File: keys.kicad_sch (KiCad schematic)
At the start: 13 parts, among them SW1 Esc, SW10 F9, SW11 F10, SW12 F11, SW13 F12, SW2 F1, SW3 F2, SW4 F3, SW5 F4, SW6 F5, SW7 F6, SW8 F7, SW9 F8

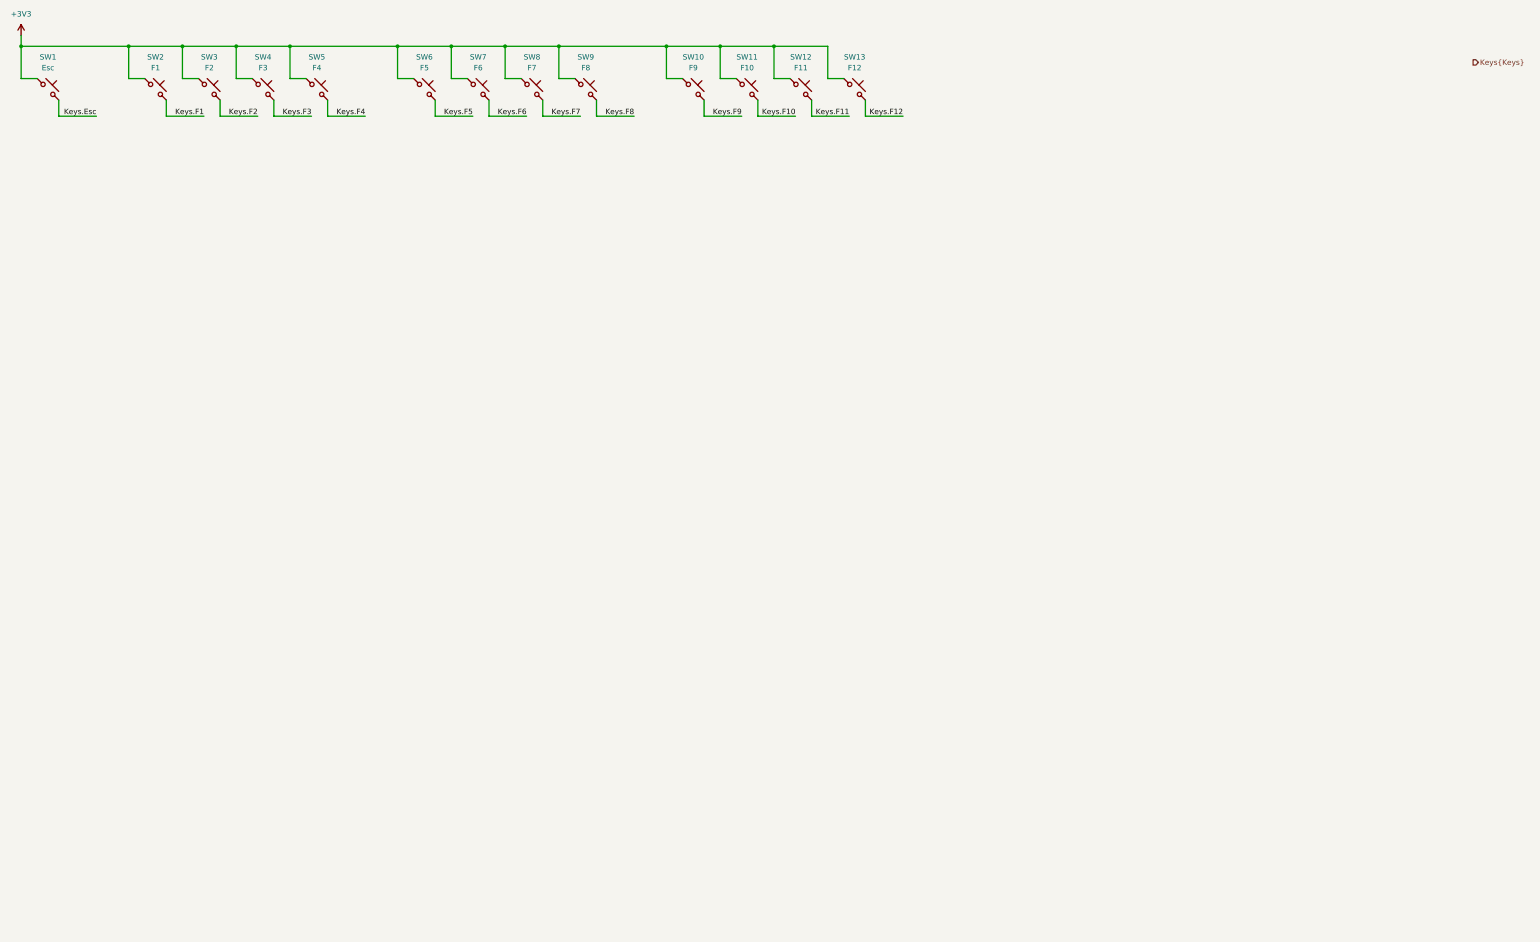
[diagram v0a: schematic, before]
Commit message: Add all keys
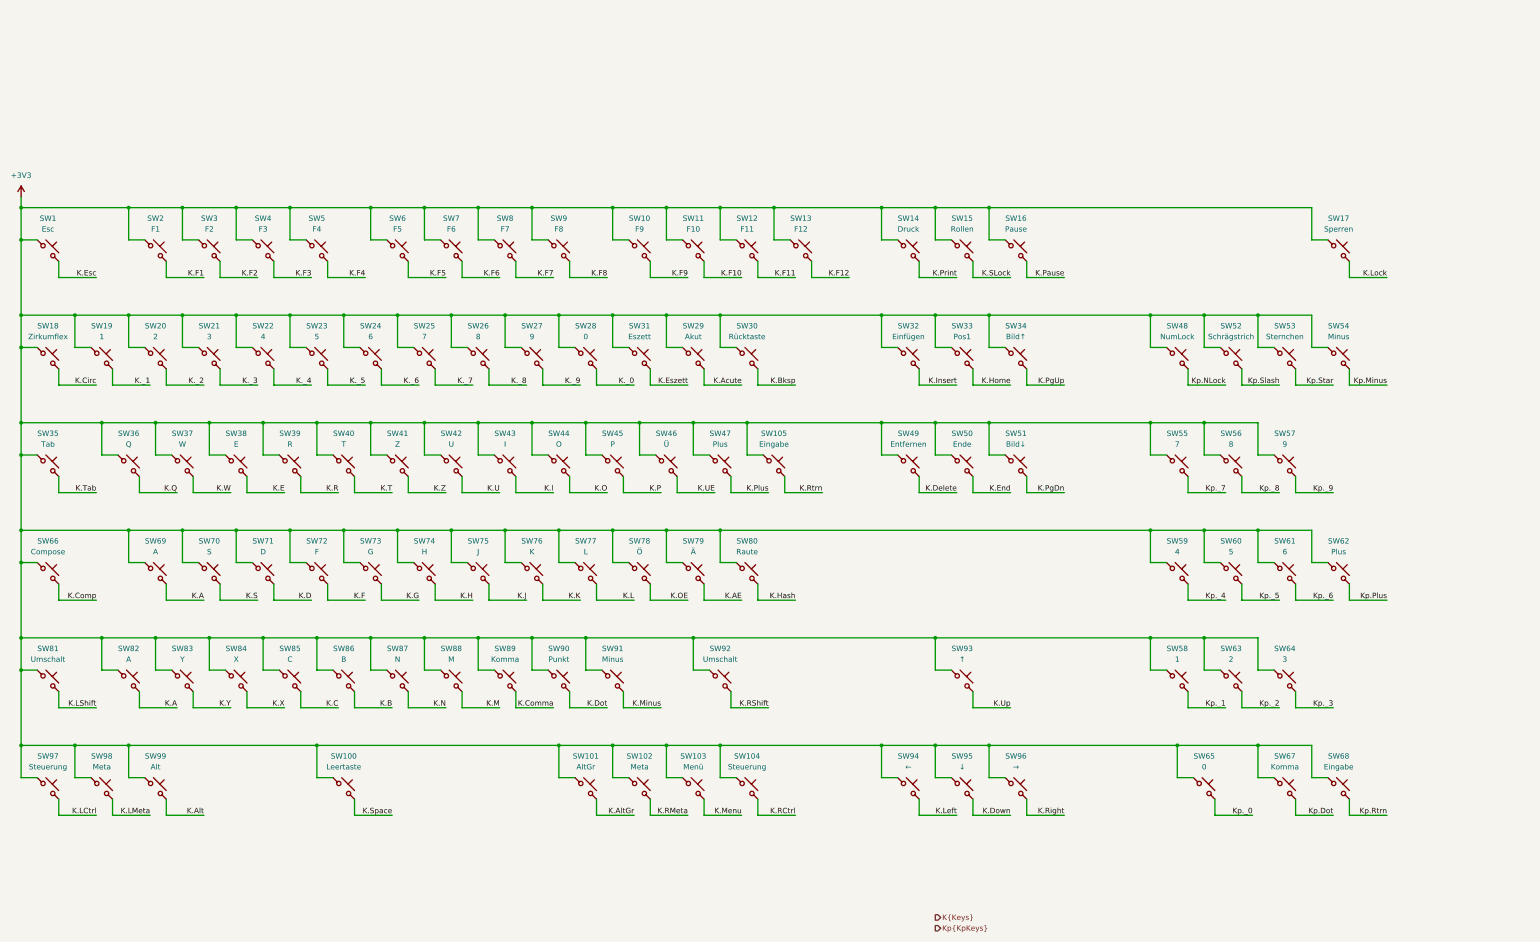
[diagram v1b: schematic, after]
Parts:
- added SW100: Leertaste, Button_Switch_Keyboard:SW_Cherry_MX_6.25u_PCB, symbol Switch:SW_Push_45deg
- added SW101: AltGr, Button_Switch_Keyboard:SW_Cherry_MX_1.25u_PCB, symbol Switch:SW_Push_45deg
- added SW102, SW98: Meta, Button_Switch_Keyboard:SW_Cherry_MX_1.25u_PCB, symbol Switch:SW_Push_45deg
- added SW103: Menü, Button_Switch_Keyboard:SW_Cherry_MX_1.25u_PCB, symbol Switch:SW_Push_45deg
- added SW104, SW97: Steuerung, Button_Switch_Keyboard:SW_Cherry_MX_1.25u_PCB, symbol Switch:SW_Push_45deg
- added SW105: Eingabe, Button_Switch_Keyboard:SW_Cherry_MX_ISOEnter_PCB, symbol Switch:SW_Push_45deg
- added SW14: Druck, Button_Switch_Keyboard:SW_Cherry_MX_1.00u_PCB, symbol Switch:SW_Push_45deg
- added SW15: Rollen, Button_Switch_Keyboard:SW_Cherry_MX_1.00u_PCB, symbol Switch:SW_Push_45deg
- added SW16: Pause, Button_Switch_Keyboard:SW_Cherry_MX_1.00u_PCB, symbol Switch:SW_Push_45deg
- added SW17: Sperren, Button_Switch_Keyboard:SW_Cherry_MX_1.00u_PCB, symbol Switch:SW_Push_45deg
- added SW18: Zirkumflex, Button_Switch_Keyboard:SW_Cherry_MX_1.00u_PCB, symbol Switch:SW_Push_45deg
- added SW19, SW58: 1, Button_Switch_Keyboard:SW_Cherry_MX_1.00u_PCB, symbol Switch:SW_Push_45deg
- added SW20, SW63: 2, Button_Switch_Keyboard:SW_Cherry_MX_1.00u_PCB, symbol Switch:SW_Push_45deg
- added SW21, SW64: 3, Button_Switch_Keyboard:SW_Cherry_MX_1.00u_PCB, symbol Switch:SW_Push_45deg
- added SW22, SW59: 4, Button_Switch_Keyboard:SW_Cherry_MX_1.00u_PCB, symbol Switch:SW_Push_45deg
- added SW23, SW60: 5, Button_Switch_Keyboard:SW_Cherry_MX_1.00u_PCB, symbol Switch:SW_Push_45deg
- added SW24, SW61: 6, Button_Switch_Keyboard:SW_Cherry_MX_1.00u_PCB, symbol Switch:SW_Push_45deg
- added SW25, SW55: 7, Button_Switch_Keyboard:SW_Cherry_MX_1.00u_PCB, symbol Switch:SW_Push_45deg
- added SW26, SW56: 8, Button_Switch_Keyboard:SW_Cherry_MX_1.00u_PCB, symbol Switch:SW_Push_45deg
- added SW27, SW57: 9, Button_Switch_Keyboard:SW_Cherry_MX_1.00u_PCB, symbol Switch:SW_Push_45deg
- added SW28: 0, Button_Switch_Keyboard:SW_Cherry_MX_1.00u_PCB, symbol Switch:SW_Push_45deg
- added SW29: Akut, Button_Switch_Keyboard:SW_Cherry_MX_1.00u_PCB, symbol Switch:SW_Push_45deg
- added SW30: Rücktaste, Button_Switch_Keyboard:SW_Cherry_MX_2.00u_PCB, symbol Switch:SW_Push_45deg
- added SW31: Eszett, Button_Switch_Keyboard:SW_Cherry_MX_1.00u_PCB, symbol Switch:SW_Push_45deg
- added SW32: Einfügen, Button_Switch_Keyboard:SW_Cherry_MX_1.00u_PCB, symbol Switch:SW_Push_45deg
- added SW33: Pos1, Button_Switch_Keyboard:SW_Cherry_MX_1.00u_PCB, symbol Switch:SW_Push_45deg
- added SW34: Bild↑, Button_Switch_Keyboard:SW_Cherry_MX_1.00u_PCB, symbol Switch:SW_Push_45deg
- added SW35: Tab, Button_Switch_Keyboard:SW_Cherry_MX_1.50u_PCB, symbol Switch:SW_Push_45deg
- added SW36: Q, Button_Switch_Keyboard:SW_Cherry_MX_1.00u_PCB, symbol Switch:SW_Push_45deg
- added SW37: W, Button_Switch_Keyboard:SW_Cherry_MX_1.00u_PCB, symbol Switch:SW_Push_45deg
- added SW38: E, Button_Switch_Keyboard:SW_Cherry_MX_1.00u_PCB, symbol Switch:SW_Push_45deg
- added SW39: R, Button_Switch_Keyboard:SW_Cherry_MX_1.00u_PCB, symbol Switch:SW_Push_45deg
- added SW40: T, Button_Switch_Keyboard:SW_Cherry_MX_1.00u_PCB, symbol Switch:SW_Push_45deg
- added SW41: Z, Button_Switch_Keyboard:SW_Cherry_MX_1.00u_PCB, symbol Switch:SW_Push_45deg
- added SW42: U, Button_Switch_Keyboard:SW_Cherry_MX_1.00u_PCB, symbol Switch:SW_Push_45deg
- added SW43: I, Button_Switch_Keyboard:SW_Cherry_MX_1.00u_PCB, symbol Switch:SW_Push_45deg
- added SW44: O, Button_Switch_Keyboard:SW_Cherry_MX_1.00u_PCB, symbol Switch:SW_Push_45deg
- added SW45: P, Button_Switch_Keyboard:SW_Cherry_MX_1.00u_PCB, symbol Switch:SW_Push_45deg
- added SW46: Ü, Button_Switch_Keyboard:SW_Cherry_MX_1.00u_PCB, symbol Switch:SW_Push_45deg
- added SW47: Plus, Button_Switch_Keyboard:SW_Cherry_MX_1.00u_PCB, symbol Switch:SW_Push_45deg
- added SW48: NumLock, Button_Switch_Keyboard:SW_Cherry_MX_1.00u_PCB, symbol Switch:SW_Push_45deg
- added SW49: Entfernen, Button_Switch_Keyboard:SW_Cherry_MX_1.00u_PCB, symbol Switch:SW_Push_45deg
- added SW50: Ende, Button_Switch_Keyboard:SW_Cherry_MX_1.00u_PCB, symbol Switch:SW_Push_45deg
- added SW51: Bild↓, Button_Switch_Keyboard:SW_Cherry_MX_1.00u_PCB, symbol Switch:SW_Push_45deg
- added SW52: Schrägstrich, Button_Switch_Keyboard:SW_Cherry_MX_1.00u_PCB, symbol Switch:SW_Push_45deg
- added SW53: Sternchen, Button_Switch_Keyboard:SW_Cherry_MX_1.00u_PCB, symbol Switch:SW_Push_45deg
- added SW54, SW91: Minus, Button_Switch_Keyboard:SW_Cherry_MX_1.00u_PCB, symbol Switch:SW_Push_45deg
- added SW62: Plus, Button_Switch_Keyboard:SW_Cherry_MX_2.00u_Vertical_PCB, symbol Switch:SW_Push_45deg
- added SW65: 0, Button_Switch_Keyboard:SW_Cherry_MX_2.00u_PCB, symbol Switch:SW_Push_45deg
- added SW66: Compose, Button_Switch_Keyboard:SW_Cherry_MX_1.75u_PCB, symbol Switch:SW_Push_45deg
- added SW67, SW89: Komma, Button_Switch_Keyboard:SW_Cherry_MX_1.00u_PCB, symbol Switch:SW_Push_45deg
- added SW68: Eingabe, Button_Switch_Keyboard:SW_Cherry_MX_2.00u_Vertical_PCB, symbol Switch:SW_Push_45deg
- added SW69, SW82: A, Button_Switch_Keyboard:SW_Cherry_MX_1.00u_PCB, symbol Switch:SW_Push_45deg
- added SW70: S, Button_Switch_Keyboard:SW_Cherry_MX_1.00u_PCB, symbol Switch:SW_Push_45deg
- added SW71: D, Button_Switch_Keyboard:SW_Cherry_MX_1.00u_PCB, symbol Switch:SW_Push_45deg
- added SW72: F, Button_Switch_Keyboard:SW_Cherry_MX_1.00u_PCB, symbol Switch:SW_Push_45deg
- added SW73: G, Button_Switch_Keyboard:SW_Cherry_MX_1.00u_PCB, symbol Switch:SW_Push_45deg
- added SW74: H, Button_Switch_Keyboard:SW_Cherry_MX_1.00u_PCB, symbol Switch:SW_Push_45deg
- added SW75: J, Button_Switch_Keyboard:SW_Cherry_MX_1.00u_PCB, symbol Switch:SW_Push_45deg
- added SW76: K, Button_Switch_Keyboard:SW_Cherry_MX_1.00u_PCB, symbol Switch:SW_Push_45deg
- added SW77: L, Button_Switch_Keyboard:SW_Cherry_MX_1.00u_PCB, symbol Switch:SW_Push_45deg
- added SW78: Ö, Button_Switch_Keyboard:SW_Cherry_MX_1.00u_PCB, symbol Switch:SW_Push_45deg
- added SW79: Ä, Button_Switch_Keyboard:SW_Cherry_MX_1.00u_PCB, symbol Switch:SW_Push_45deg
- added SW80: Raute, Button_Switch_Keyboard:SW_Cherry_MX_1.00u_PCB, symbol Switch:SW_Push_45deg
- added SW81: Umschalt, Button_Switch_Keyboard:SW_Cherry_MX_1.25u_PCB, symbol Switch:SW_Push_45deg
- added SW83: Y, Button_Switch_Keyboard:SW_Cherry_MX_1.00u_PCB, symbol Switch:SW_Push_45deg
- added SW84: X, Button_Switch_Keyboard:SW_Cherry_MX_1.00u_PCB, symbol Switch:SW_Push_45deg
- added SW85: C, Button_Switch_Keyboard:SW_Cherry_MX_1.00u_PCB, symbol Switch:SW_Push_45deg
- added SW86: B, Button_Switch_Keyboard:SW_Cherry_MX_1.00u_PCB, symbol Switch:SW_Push_45deg
- added SW87: N, Button_Switch_Keyboard:SW_Cherry_MX_1.00u_PCB, symbol Switch:SW_Push_45deg
- added SW88: M, Button_Switch_Keyboard:SW_Cherry_MX_1.00u_PCB, symbol Switch:SW_Push_45deg
- added SW90: Punkt, Button_Switch_Keyboard:SW_Cherry_MX_1.00u_PCB, symbol Switch:SW_Push_45deg
- added SW92: Umschalt, Button_Switch_Keyboard:SW_Cherry_MX_2.75u_PCB, symbol Switch:SW_Push_45deg
- added SW93: ↑, Button_Switch_Keyboard:SW_Cherry_MX_1.00u_PCB, symbol Switch:SW_Push_45deg
- added SW94: ←, Button_Switch_Keyboard:SW_Cherry_MX_1.00u_PCB, symbol Switch:SW_Push_45deg
- added SW95: ↓, Button_Switch_Keyboard:SW_Cherry_MX_1.00u_PCB, symbol Switch:SW_Push_45deg
- added SW96: →, Button_Switch_Keyboard:SW_Cherry_MX_1.00u_PCB, symbol Switch:SW_Push_45deg
- added SW99: Alt, Button_Switch_Keyboard:SW_Cherry_MX_1.25u_PCB, symbol Switch:SW_Push_45deg
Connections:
- net +3V3: now also SW100.1, SW101.1, SW102.1, SW103.1, SW104.1, SW105.1, SW14.1, SW15.1, SW16.1, SW17.1, SW18.1, SW19.1, SW20.1, SW21.1, SW22.1, SW23.1, SW24.1, SW25.1, SW26.1, SW27.1, SW28.1, SW29.1, SW30.1, SW31.1, SW32.1, SW33.1, SW34.1, SW35.1, SW36.1, SW37.1, SW38.1, SW39.1, SW40.1, SW41.1, SW42.1, SW43.1, SW44.1, SW45.1, SW46.1, SW47.1, SW48.1, SW49.1, SW50.1, SW51.1, SW52.1, SW53.1, SW54.1, SW55.1, SW56.1, SW57.1, SW58.1, SW59.1, SW60.1, SW61.1, SW62.1, SW63.1, SW64.1, SW65.1, SW66.1, SW67.1, SW68.1, SW69.1, SW70.1, SW71.1, SW72.1, SW73.1, SW74.1, SW75.1, SW76.1, SW77.1, SW78.1, SW79.1, SW80.1, SW81.1, SW82.1, SW83.1, SW84.1, SW85.1, SW86.1, SW87.1, SW88.1, SW89.1, SW90.1, SW91.1, SW92.1, SW93.1, SW94.1, SW95.1, SW96.1, SW97.1, SW98.1, SW99.1
- net Keys.Esc renamed K.Esc
- net Keys.F1 renamed K.F1
- net Keys.F10 renamed K.F10
- net Keys.F11 renamed K.F11
- net Keys.F12 renamed K.F12
- net Keys.F2 renamed K.F2
- net Keys.F3 renamed K.F3
- net Keys.F4 renamed K.F4
- net Keys.F5 renamed K.F5
- net Keys.F6 renamed K.F6
- net Keys.F7 renamed K.F7
- net Keys.F8 renamed K.F8
- net Keys.F9 renamed K.F9
- new net K.A: SW69.2, SW82.2
- new net K.AE: SW79.2
- new net K.Acute: SW29.2
- new net K.Alt: SW99.2
- new net K.AltGr: SW101.2
- new net K.B: SW86.2
- new net K.Bksp: SW30.2
- new net K.C: SW85.2
- new net K.Circ: SW18.2
- new net K.Comma: SW89.2
- new net K.Comp: SW66.2
- new net K.D: SW71.2
- new net K.Delete: SW49.2
- new net K.Dot: SW90.2
- new net K.Down: SW95.2
- new net K.E: SW38.2
- new net K.End: SW50.2
- new net K.Eszett: SW31.2
- new net K.F: SW72.2
- new net K.G: SW73.2
- new net K.H: SW74.2
- new net K.Hash: SW80.2
- new net K.Home: SW33.2
- new net K.I: SW43.2
- new net K.Insert: SW32.2
- new net K.J: SW75.2
- new net K.K: SW76.2
- new net K.L: SW77.2
- new net K.LCtrl: SW97.2
- new net K.LMeta: SW98.2
- new net K.LShift: SW81.2
- new net K.Left: SW94.2
- new net K.Lock: SW17.2
- new net K.M: SW88.2
- new net K.Menu: SW103.2
- new net K.Minus: SW91.2
- new net K.N: SW87.2
- new net K.O: SW44.2
- new net K.OE: SW78.2
- new net K.P: SW45.2
- new net K.Pause: SW16.2
- new net K.PgDn: SW51.2
- new net K.PgUp: SW34.2
- new net K.Plus: SW47.2
- new net K.Print: SW14.2
- new net K.Q: SW36.2
- new net K.R: SW39.2
- new net K.RCtrl: SW104.2
- new net K.RMeta: SW102.2
- new net K.RShift: SW92.2
- new net K.Right: SW96.2
- new net K.Rtrn: SW105.2
- new net K.S: SW70.2
- new net K.SLock: SW15.2
- new net K.Space: SW100.2
- new net K.T: SW40.2
- new net K.Tab: SW35.2
- new net K.U: SW42.2
- new net K.UE: SW46.2
- new net K.Up: SW93.2
- new net K.W: SW37.2
- new net K.X: SW84.2
- new net K.Y: SW83.2
- new net K.Z: SW41.2
- new net K._0: SW28.2
- new net K._1: SW19.2
- new net K._2: SW20.2
- new net K._3: SW21.2
- new net K._4: SW22.2
- new net K._5: SW23.2
- new net K._6: SW24.2
- new net K._7: SW25.2
- new net K._8: SW26.2
- new net K._9: SW27.2
- new net Kp.Dot: SW67.2
- new net Kp.Minus: SW54.2
- new net Kp.NLock: SW48.2
- new net Kp.Plus: SW62.2
- new net Kp.Rtrn: SW68.2
- new net Kp.Slash: SW52.2
- new net Kp.Star: SW53.2
- new net Kp._0: SW65.2
- new net Kp._1: SW58.2
- new net Kp._2: SW63.2
- new net Kp._3: SW64.2
- new net Kp._4: SW59.2
- new net Kp._5: SW60.2
- new net Kp._6: SW61.2
- new net Kp._7: SW55.2
- new net Kp._8: SW56.2
- new net Kp._9: SW57.2
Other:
- moved on the sheet: SW1, SW10, SW11, SW12, SW13, SW2, SW3, SW4, SW5, SW6, SW7, SW8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

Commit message: Initial commit of the PCB
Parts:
- added SW81: V, Button_Switch_Keyboard:SW_Cherry_MX_1.00u_PCB, symbol Switch:SW_Push_45deg
- SW77: renamed from SW82; value A -> <
- renumbered SW104 to SW100, SW94 to SW101, SW95 to SW102, SW96 to SW103, SW65 to SW104, SW67 to SW105, SW68 to SW106, SW31 to SW29, SW29 to SW30, SW30 to SW31, SW48 to SW35, SW52 to SW36, SW53 to SW37, SW54 to SW38, SW35 to SW39, SW36 to SW40, SW37 to SW41, SW38 to SW42, SW39 to SW43, SW40 to SW44, SW41 to SW45, SW42 to SW46, SW43 to SW47, SW44 to SW48, SW45 to SW49, SW46 to SW50, SW47 to SW51, SW105 to SW52, SW49 to SW53, SW50 to SW54, SW51 to SW55, SW55 to SW56, SW56 to SW57, SW57 to SW58, SW66 to SW59, SW69 to SW60, SW70 to SW61, SW71 to SW62, SW72 to SW63, SW73 to SW64, SW74 to SW65, SW75 to SW66, SW76 to SW67, SW77 to SW68, SW78 to SW69, SW79 to SW70, SW80 to SW71, SW59 to SW72, SW60 to SW73, SW61 to SW74, SW62 to SW75, SW81 to SW76, SW83 to SW78, SW84 to SW79, SW85 to SW80, SW86 to SW82, SW87 to SW83, SW88 to SW84, SW89 to SW85, SW90 to SW86, SW91 to SW87, SW92 to SW88, SW93 to SW89, SW58 to SW90, SW63 to SW91, SW64 to SW92, SW97 to SW93, SW98 to SW94, SW99 to SW95, SW100 to SW96, SW101 to SW97, SW102 to SW98, SW103 to SW99
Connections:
- net +3V3: now also SW81.1
- net K.A: no longer SW77.2
- new net K.Lt: SW77.2
- new net K.V: SW81.2
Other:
- moved on the sheet: SW82, SW83, SW84, SW85, SW86, SW87
